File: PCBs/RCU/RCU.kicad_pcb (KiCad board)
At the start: 4 copper layers, 99 x 139 mm, 148 parts, among them J100 Conn_01x02, J200 USB_C_Receptacle_USB2.0, J201 Conn_01x05, J300 Right_Motor_Screw_Terminal, J301 Right_Encoder_Conn, J302 Left_Motor_Screw_Terminal, J303 Left_Encoder_Conn, J400 USB_C_Receptacle_USB2.0, Q400 2N7002NXAKR (NMOS), Q401 2N7002NXAKR (NMOS), Q402 BSS84AK,215 (PMOS), Q403 2N7002NXAKR (NMOS), SW201 SW_Push, SW400 SW_Push, SW401 SW_SPDT, U100 LM2576S-ADJ, U101 AP63203WU, U102 AZ1117-3.3, U200 STM32G0B1CBT6, U201 USBLC6-2SC6, U300 OPA320, U301 DRV8876, U302 OPA320, U303 DRV8876, U400 USBLC6-2SC6, U401 CH340C, U402 ESP32-MINI-1, U403 DG2788ADN-T1-GE4, U500 APDS-9306-065, U501 LSM6DS3, U502 SHT30-DIS, U600 ADC121C027CIMK/NOPB, U601 OPA320, U602 ADC121C027CIMK/NOPB, U603 OPA320, U700 SST26VF032BT-104I/SM, Y200 16MHz

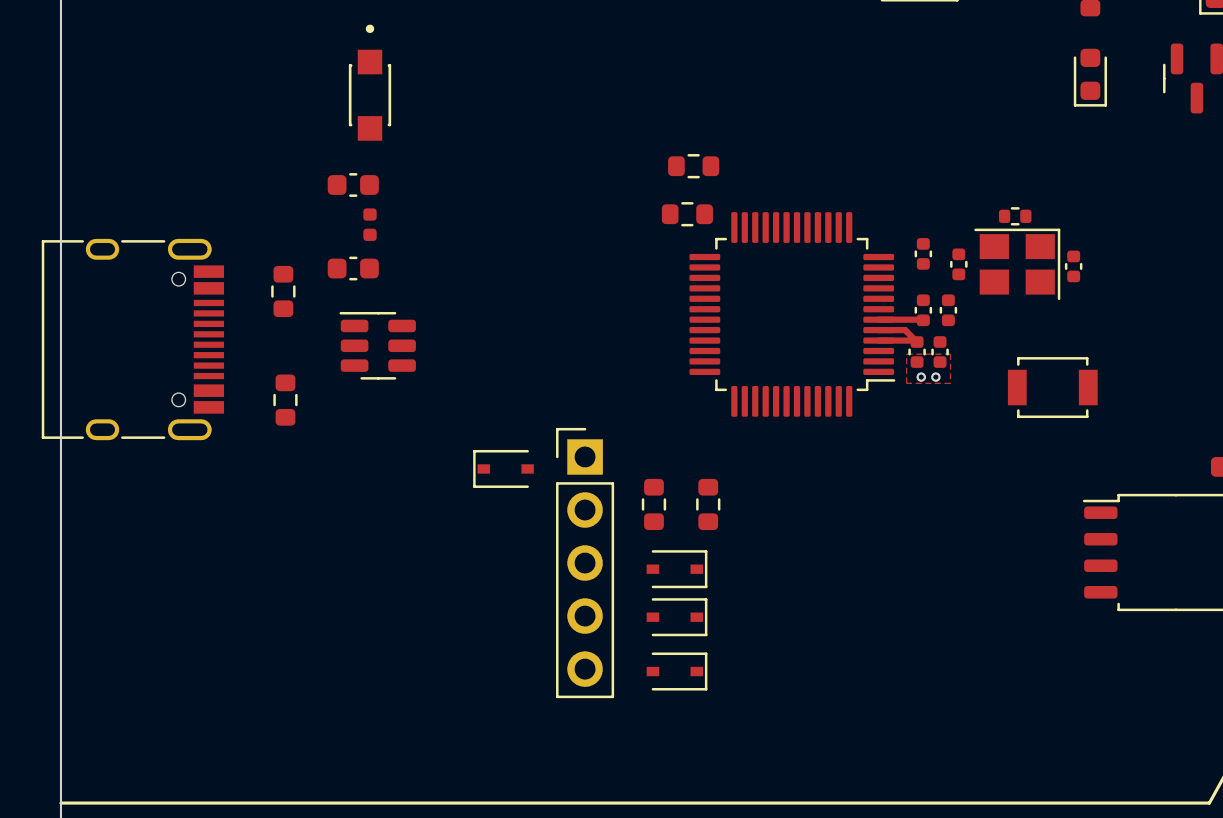
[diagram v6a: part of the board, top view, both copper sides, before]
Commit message: traced USB circuitry
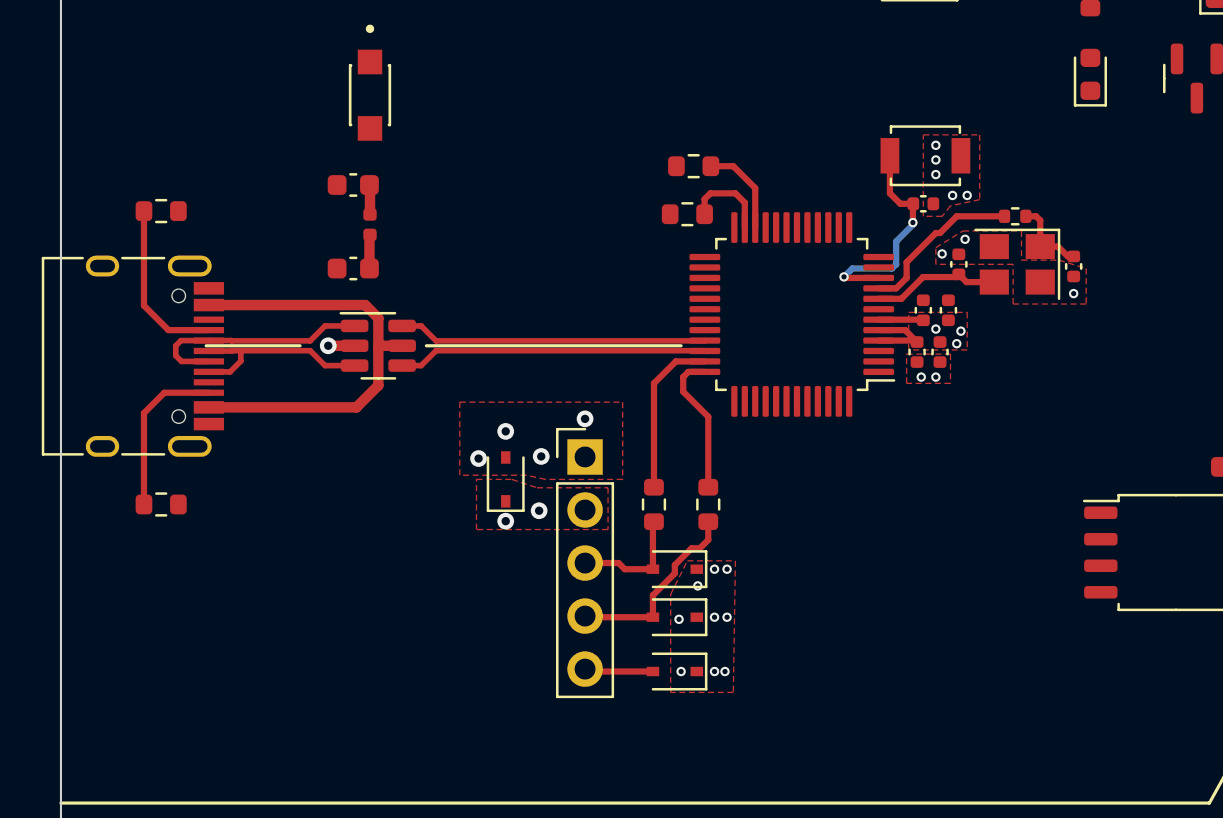
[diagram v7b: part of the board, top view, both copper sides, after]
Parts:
- moved SW201 12.7 mm to (109.4, 70.0)
- moved R206 7.77 mm to (72.8, 86.7), turned to 180 degrees
- moved R205 7.01 mm to (72.8, 72.7), turned to 0 degrees
- moved C206 2.40 mm to (109.3, 72.3), turned to 0 degrees
- moved J200 0.80 mm to (71.0, 79.6)
- moved D200 0.50 mm to (89.3, 85.5), turned to 90 degrees
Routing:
- net /[2] Microcontroller/VBUS1: track 0.00 -> 21.3 mm
- net /[2] Microcontroller/Prot_D-: track 0.00 -> 14.8 mm
- net /[2] Microcontroller/Prot_D+: track 0.00 -> 14.8 mm
- net /[2] Microcontroller/NRST: track 0.00 -> 14.1 mm, vias 0 -> 2
- net /[2] Microcontroller/D-: track 0.00 -> 11.1 mm
- net /[2] Microcontroller/D+: track 0.00 -> 9.52 mm
- net /[2] Microcontroller/SWCLK: track 0.00 -> 9.18 mm
- net /[2] Microcontroller/CC1: track 0.00 -> 8.12 mm
- net /[2] Microcontroller/HSE_OUT: track 0.00 -> 7.90 mm
- net /[2] Microcontroller/CC2: track 0.00 -> 7.89 mm
- net /[2] Microcontroller/SWDIO_Pin: track 0.00 -> 7.85 mm
- net /[2] Microcontroller/SWCLK_Pin: track 0.00 -> 6.91 mm
- net /[2] Microcontroller/HSE_IN: track 0.00 -> 6.18 mm
- net /[2] Microcontroller/SWDIO: track 0.00 -> 5.67 mm
- net I2C_SDA: track 0.00 -> 4.45 mm
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- added copper zone on F.Cu, net +3V3

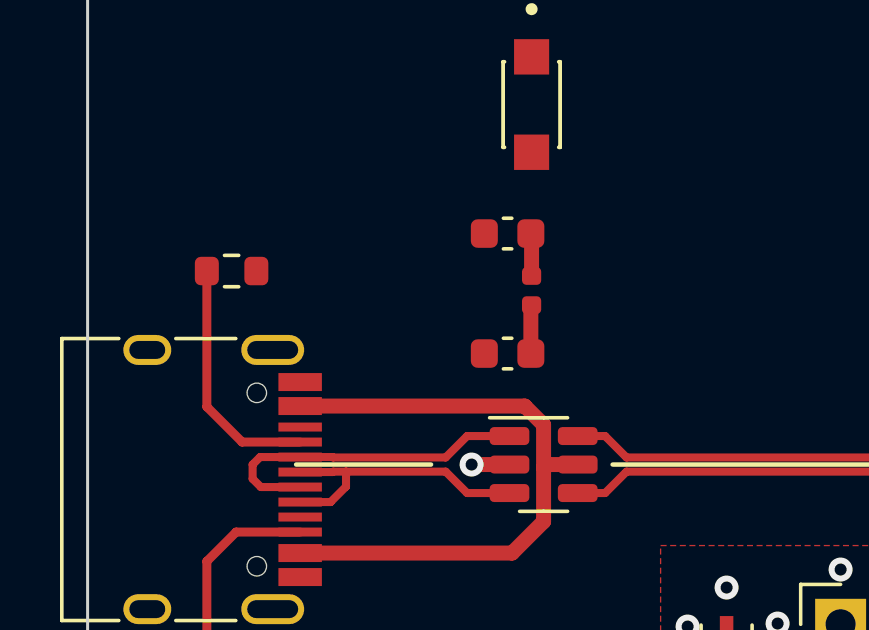
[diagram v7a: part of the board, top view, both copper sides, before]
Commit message: Changed VBUS1 and VBUS2 from net labels to global labels
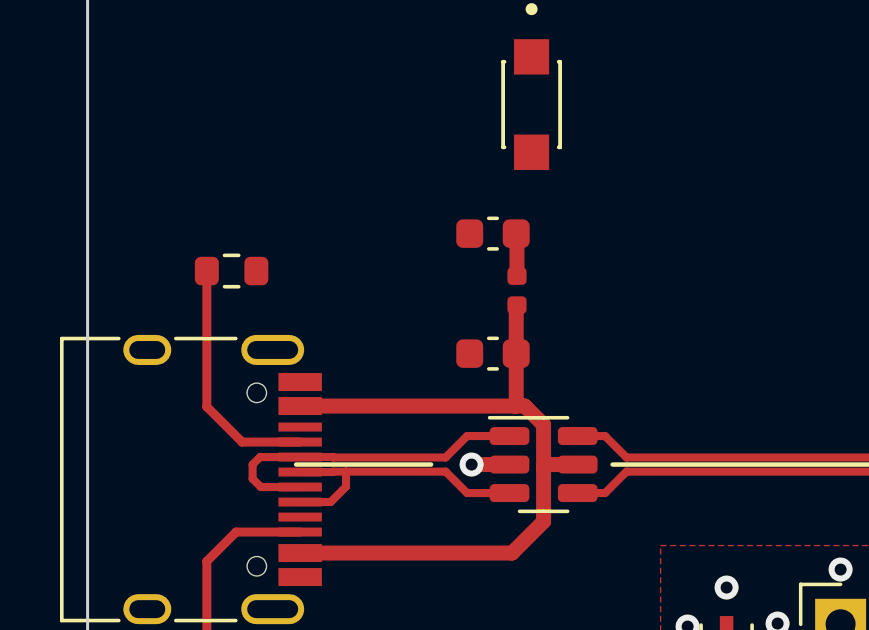
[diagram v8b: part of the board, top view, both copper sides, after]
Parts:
- moved C107 0.49 mm to (81.5, 75.4)
- moved C108 0.49 mm to (81.5, 71.4)
- moved L102 0.49 mm to (82.3, 73.3)
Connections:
- C107 pad 1: /[1] Power/VBUS1 -> VBUS1
- J200 pad A4: /[2] Microcontroller/VBUS1 -> VBUS1
- J200 pad A9: /[2] Microcontroller/VBUS1 -> VBUS1
- J200 pad B4: /[2] Microcontroller/VBUS1 -> VBUS1
- J200 pad B9: /[2] Microcontroller/VBUS1 -> VBUS1
- L102 pad 1: /[1] Power/VBUS1 -> VBUS1
- U201 pad 5: /[2] Microcontroller/VBUS1 -> VBUS1
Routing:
- net VBUS1: track 0.00 -> 24.7 mm
- net /[2] Microcontroller/VBUS1: track 21.3 -> 0.00 mm
- net /[1] Power/VBUS1: track 1.63 -> 0.00 mm
